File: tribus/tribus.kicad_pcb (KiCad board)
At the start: 2 copper layers, 30 x 106 mm, 111 parts, among them J1 PWR, J4 Conn_01x08_Female, J7 Conn_01x08_Male, Q1 MMBT3904, Q2 MMBT3904, Q3 MMBT3904, Q4 MMBT3904, Q5 MMBT3904, Q6 MMBT3904, U1 78L05, U2 TL074, U3 LM324

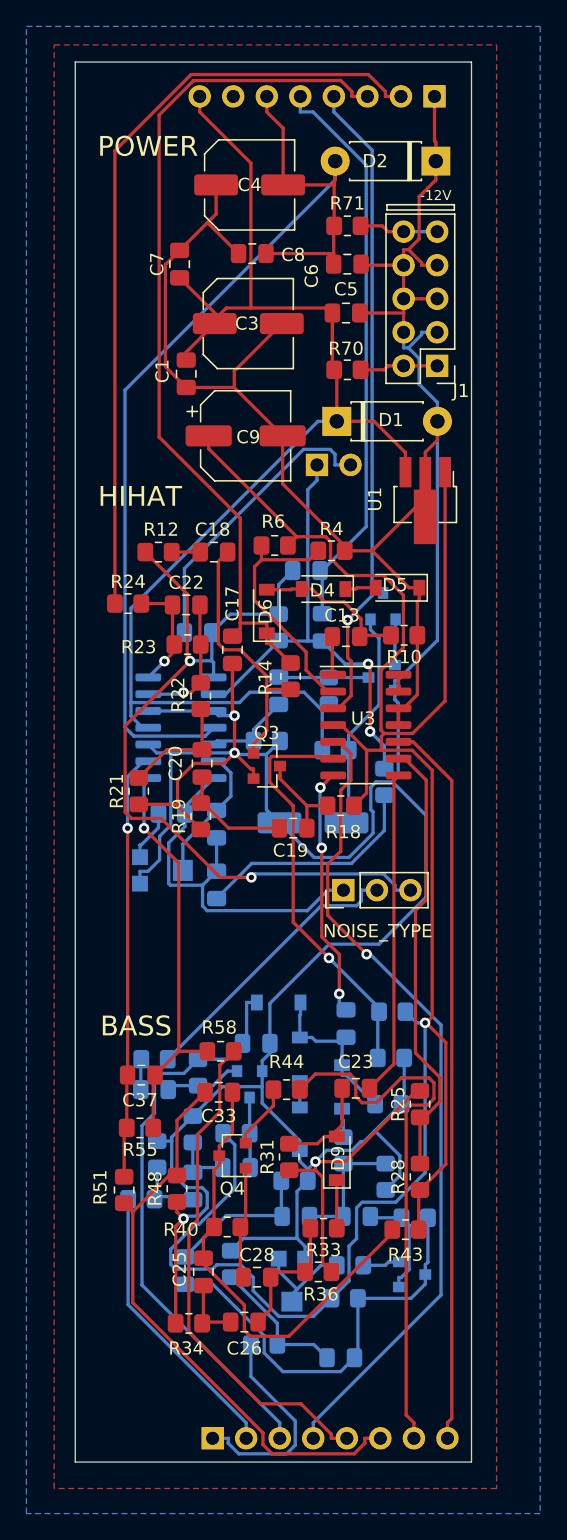
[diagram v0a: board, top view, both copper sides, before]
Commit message: Fix wrong resistor value, add routes
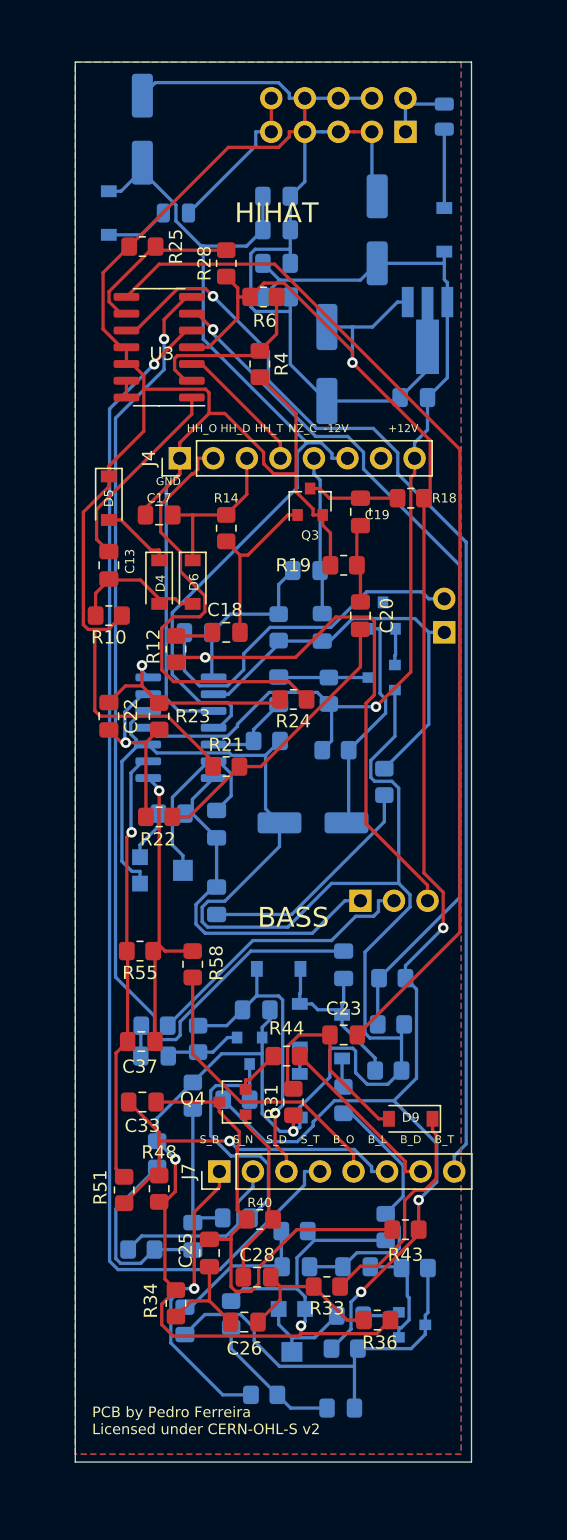
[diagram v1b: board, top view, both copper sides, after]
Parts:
- removed R70, R71: 10, Resistor_SMD:R_0805_2012Metric_Pad1.20x1.40mm_HandSolder
- added L1: L_Small, Capacitor_SMD:C_0805_2012Metric, B.Cu at (27.9, 4.13)
- added L2: L_Small, Capacitor_SMD:C_0805_2012Metric, B.Cu at (7.62, 11.4)
- added REF**: OSHW-Logo2_7.3x6mm_SilkScreen, Symbol:OSHW-Logo2_7.3x6mm_SilkScreen, B.Cu at (5.08, 101.6)
- C1, C3, C4, C5, C6, C7, C8, C9, NOISE_TYPE, U1: moved to B.Cu
- D1, D2: value 1N4001 -> 1N5819; footprint Diode_THT:D_DO-41_SOD81_P7.62mm_Horizontal -> Diode_SMD:D_SOD-123; moved to B.Cu
- J1: value PWR -> Conn_02x05_Odd_Even; moved to B.Cu
- J4, J7: moved to F.Cu
- R55: value 15K -> 100K
- moved R28 70.7 mm to (11.4, 15.2)
- moved R25 68.2 mm to (5.08, 14.0), turned to 180 degrees
- moved U3 32.6 mm to (6.35, 21.6), turned to 180 degrees
- moved J4 29.3 mm to (16.8, 30.0)
- moved D2 25.1 mm to (2.54, 11.4), turned to 90 degrees
- moved C19 24.5 mm to (21.6, 34.1), turned to 90 degrees
- moved R18 23.9 mm to (25.4, 33.0)
- moved D5 22.9 mm to (2.54, 33.0), turned to 270 degrees
- moved R10 22.4 mm to (2.54, 41.9)
- moved J7 22.3 mm to (19.8, 84.0), turned to 90 degrees
- moved R19 21.9 mm to (20.3, 38.1), turned to 0 degrees
- moved Q3 20.3 mm to (17.8, 33.3), turned to 90 degrees
- moved R6 18.8 mm to (14.2, 17.8), turned to 0 degrees
- moved C13 18.8 mm to (2.54, 38.1), turned to 90 degrees
- moved J1 17.9 mm to (25.0, 5.28), turned to 90 degrees
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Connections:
- D1 pad 2: GND -> Net-(D1-Pad2)
- D2 pad 1: GND -> Net-(D2-Pad1)
- J4 pad 7: (no net) -> Net-(J4-Pad7)
- Q1 pad 3: (no net) -> Net-(Q1-Pad3)
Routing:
- net GND: track 337.8 -> 401.5 mm, vias 4 -> 3
- net Net-(C24-Pad2): track 19.0 -> 77.5 mm, vias 3 -> 1
- net Net-(C23-Pad2): track 24.6 -> 79.6 mm
- net HH_DECAY_BACK: track 65.8 -> 12.4 mm
- net HH_TRIG_BACK: track 49.2 -> 10.4 mm, vias 1 -> 0
- net Net-(R27-Pad1): track 31.1 -> 66.5 mm
- net +5V: track 162.4 -> 130.1 mm, vias 1 -> 4
- net NOISE_CUTOFF_BACK: track 43.3 -> 12.0 mm
- net SNARE_TRIGGER_BACK: track 62.0 -> 93.2 mm
- net BASS_TRIG_BACK: track 55.2 -> 85.2 mm, vias 0 -> 1
- net BASS_DECAY_BACK: track 42.0 -> 13.2 mm
- net +12V: track 101.5 -> 76.4 mm, vias 0 -> 1
- net HH_OUT_BACK: track 59.2 -> 34.2 mm
- net Net-(R25-Pad1): track 33.7 -> 12.9 mm
- net SNARE_DECAY_BACK: track 43.6 -> 23.1 mm, vias 0 -> 1
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- added copper zone on B.Cu, net (none)
- added copper zone on F.Cu, net (none)
- removed copper zone on B.Cu, net GND
- removed copper zone on F.Cu, net GND
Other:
- board text added: "+12V"
- board text added: "B_D"
- board text added: "B_L"
- board text added: "B_O"
- board text added: "B_T"
- board text added: "Based on the Korg Monotribe Drums"
- board text added: "GND"
- board text added: "HH_D"
- board text added: "HH_O"
- board text added: "HH_T"
- board text added: "NZ_C"
- board text added: "PCB by Pedro Ferreira Licensed under CERN-OHL-S v2"
- board text added: "S_B"
- board text added: "S_D"
- board text added: "S_N"
- board text added: "S_T"
- board text added: "Tribus"
- board text added: "https://bit.ly/2OCx7gC"

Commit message: Make ELFO nicer, fix issues
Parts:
- added REF**: KiCad-Logo2_5mm_SilkScreen, Symbol:KiCad-Logo2_5mm_SilkScreen, F.Cu at (25.4, 54.6)
- C2, C3, C4: footprint Capacitor_SMD:C_Elec_6.3x5.8 -> Capacitor_SMD:CP_Elec_4x5.4
- C9: footprint Capacitor_SMD:CP_Elec_6.3x5.9 -> Capacitor_SMD:CP_Elec_4x5.4
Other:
- board text added: "PCB by Pedro Ferreira Licensed under CERN-OHL-P v2"
- board text removed: "PCB by Pedro Ferreira Licensed under CERN-OHL-S v2"

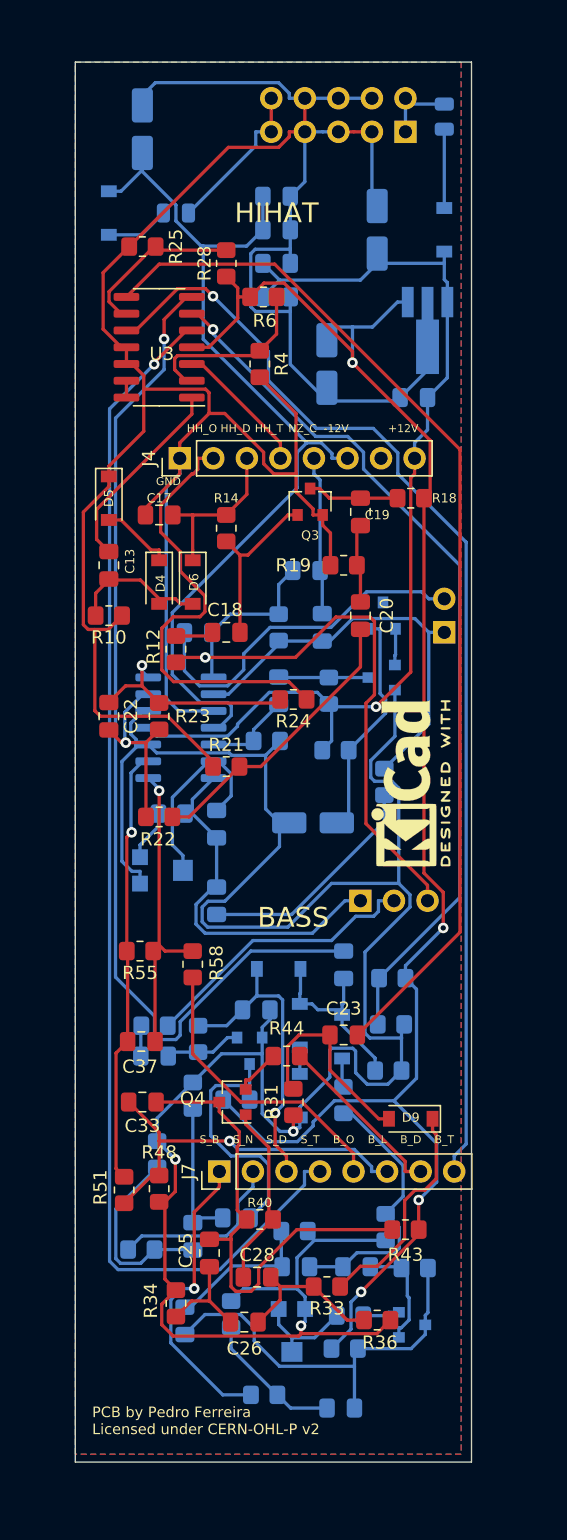
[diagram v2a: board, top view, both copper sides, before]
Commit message: Use 1206 resistors, because I messed up :facepalm:
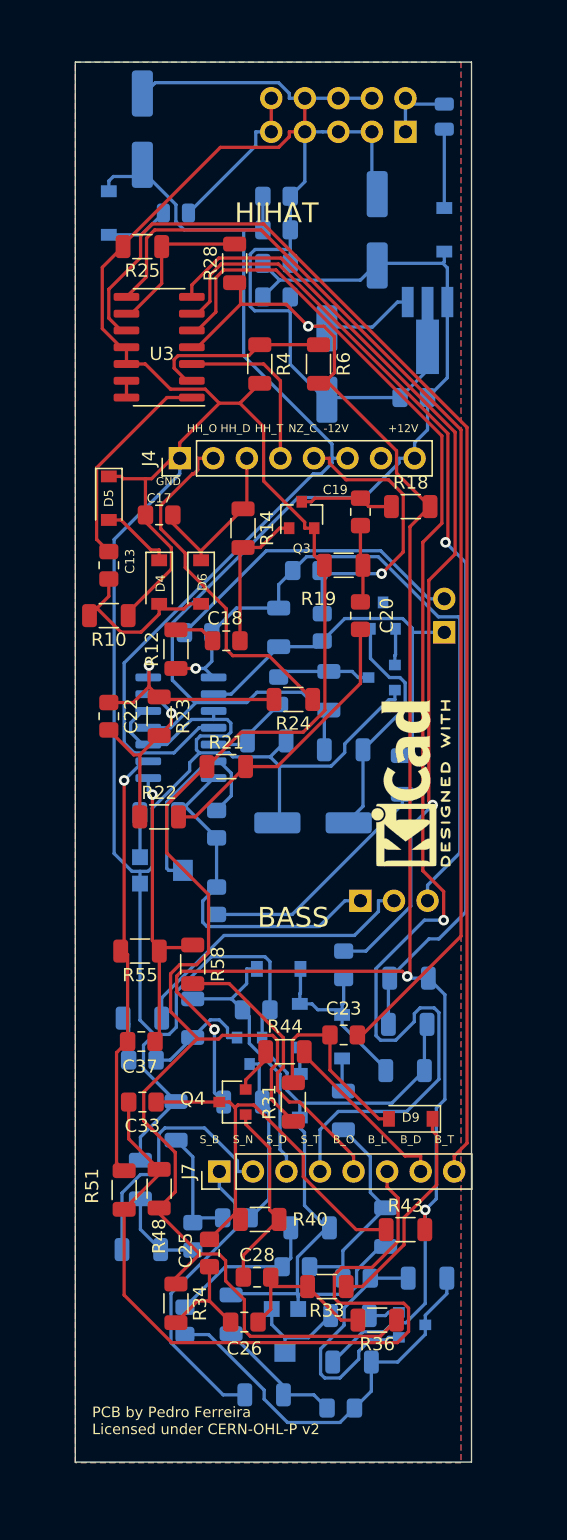
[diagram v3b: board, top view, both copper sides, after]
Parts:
- C2, C3, C4, C9: footprint Capacitor_SMD:CP_Elec_4x5.4 -> Capacitor_SMD:CP_Elec_6.3x5.8
- R1, R10, R11, R12, R14, R18, R19, R2, R21, R22, R23, R24, R25, R27, R28, R3, R30, R31, R32, R33, R34, R35, R36, R37, R38, R39, R4, R40, R41, R42, R43, R44, R45, R46, R47, R48, R49, R5, R50, R51, R52, R53, R54, R55, R58, R6, R9: footprint Resistor_SMD:R_0805_2012Metric_Pad1.20x1.40mm_HandSolder -> Resistor_SMD:R_1206_3216Metric
- moved R6 6.58 mm to (18.4, 22.9), turned to 90 degrees
- moved R49 2.29 mm to (7.63, 80.2)
- moved R52 2.29 mm to (4.93, 84.6)
- moved R41 1.62 mm to (8.89, 72.4)
- moved R9 1.46 mm to (24.8, 54.0)
- moved R27 1.27 mm to (25.2, 72.9)
- moved R14 1.27 mm to (12.7, 35.3)
- moved R30 1.27 mm to (25.3, 69.4)
- moved R32 1.27 mm to (25.0, 76.4)
- moved R42 1.24 mm to (26.7, 92.1)
- moved R37 1.21 mm to (17.8, 88.3)
- moved Q3 1.18 mm to (17.1, 34.3)
- moved R46 1.16 mm to (21.0, 98.4)
- moved R38 1.08 mm to (5.08, 72.4)
- moved C31 0.97 mm to (5.08, 75.6)
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- renumbered REF** to KICADLOGO, REF** to OSHWLOGO
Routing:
- net GND: track 401.5 -> 441.4 mm, vias 3 -> 0
- net BASS_LED_BACK: track 28.5 -> 61.0 mm, vias 1 -> 0
- net +5V: track 130.1 -> 143.2 mm
- net BASS_TRIG_BACK: track 85.2 -> 97.2 mm, vias 1 -> 0
- net Net-(C32-Pad1): track 8.32 -> 19.4 mm
- net NOISE_CUTOFF_BACK: track 12.0 -> 22.6 mm, vias 0 -> 1
- net Net-(R27-Pad1): track 66.5 -> 75.7 mm
- net SNARE_TRIGGER_BACK: track 93.2 -> 102.4 mm
- net Net-(C36-Pad1): track 14.6 -> 6.93 mm
- net HH_OUT_BACK: track 34.2 -> 27.0 mm
- net Net-(C24-Pad2): track 77.5 -> 71.1 mm
- net SNARE_NOISE_BACK: track 13.6 -> 19.5 mm
- net Net-(C34-Pad2): track 19.1 -> 13.3 mm
- net +12V: track 76.4 -> 82.1 mm, vias 1 -> 0
- net -12V: track 70.6 -> 76.1 mm
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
